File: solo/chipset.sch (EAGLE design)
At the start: 24 parts

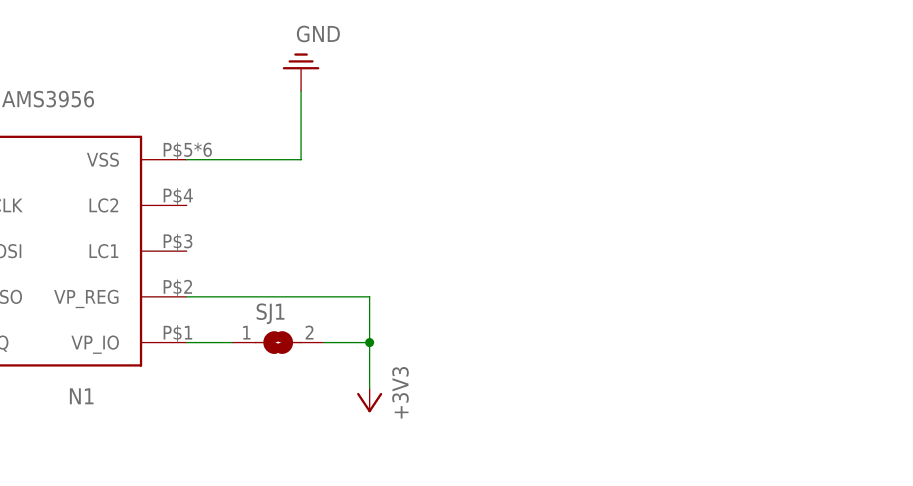
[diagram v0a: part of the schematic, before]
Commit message: add molex nfc antenna/coil
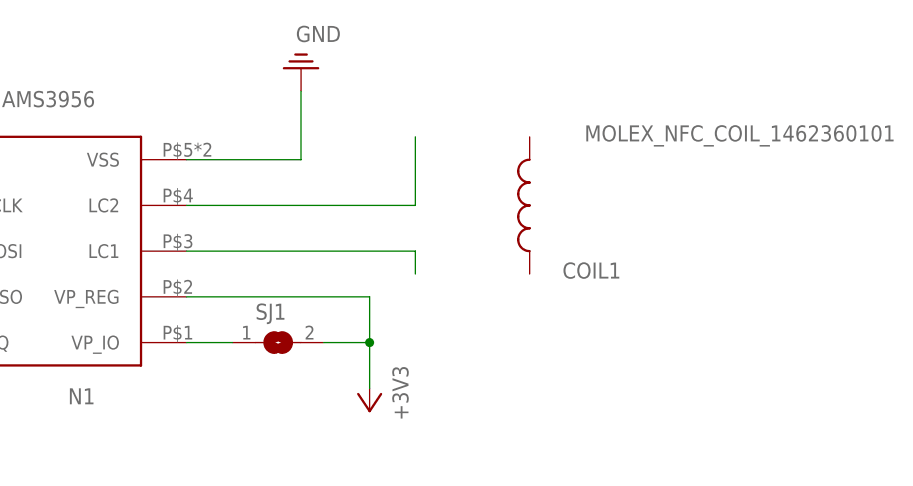
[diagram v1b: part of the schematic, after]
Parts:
- added COIL1: MOLEX_NFC_COIL_1462360101, efm-fido:MOLEX_NFC_COIL_1462360101
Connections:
- new net N$12: N1.LC2
- new net N$13: N1.LC1
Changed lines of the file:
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@@
 <part name="SWCLK" library="efm-fido" library_urn="urn:adsk.eagle:library:4245354" deviceset="TEST_POINT" device="" package3d_urn="urn:adsk.eagle:package:4245792/4"/>
 <part name="R1" library="efm-fido" library_urn="urn:adsk.eagle:library:4245354" deviceset="RESISTOR" device="" package3d_urn="urn:adsk.eagle:package:4245807/6" value="175"/>
-<part name="L1" library="efm-fido" library_urn="urn:adsk.eagle:library:4245354" deviceset="EAST1616RGBA3-LED-RGB" device="CL-505S-X-SD-T" package3d_urn="urn:adsk.eagle:package:4878740/4"/>
+<part name="L1" library="efm-fido" library_urn="urn:adsk.eagle:library:4245354" deviceset="EAST1616RGBA3-LED-RGB" device="CL-505S-X-SD-T" package3d_urn="urn:adsk.eagle:package:4878740/6"/>
 <part name="STX-&gt;" library="efm-fido" library_urn="urn:adsk.eagle:library:4245354" deviceset="TEST_POINT" device="" package3d_urn="urn:adsk.eagle:package:4245792/4"/>
 <part name="SRX&lt;-" library="efm-fido" library_urn="urn:adsk.eagle:library:4245354" deviceset="TEST_POINT" device="" package3d_urn="urn:adsk.eagle:package:4245792/4"/>
@@
 <part name="C6" library="efm-fido" library_urn="urn:adsk.eagle:library:4245354" deviceset="CAPACITOR" device="" package3d_urn="urn:adsk.eagle:package:4245806/7" value="4.7u"/>
 <part name="SUPPLY6" library="supply2" library_urn="urn:adsk.eagle:library:372" deviceset="PE" device="" value="GND"/>
-<part name="ST1" library="efm-fido" library_urn="urn:adsk.eagle:library:4245354" deviceset="STM32L432KCU6" device="" package3d_urn="urn:adsk.eagle:package:4245373/4"/>
+<part name="ST1" library="efm-fido" library_urn="urn:adsk.eagle:library:4245354" deviceset="STM32L432KCU6" device="" package3d_urn="urn:adsk.eagle:package:4245373/6"/>
 <part name="SWO" library="efm-fido" library_urn="urn:adsk.eagle:library:4245354" deviceset="TEST_POINT" device="" package3d_urn="urn:adsk.eagle:package:4245792/4"/>
-<part name="L3" library="efm-fido" library_urn="urn:adsk.eagle:library:4245354" deviceset="NCP114AMX330TCG" device="" package3d_urn="urn:adsk.eagle:package:5621121/2"/>
+<part name="L3" library="efm-fido" library_urn="urn:adsk.eagle:library:4245354" deviceset="NCP114AMX330TCG" device="" package3d_urn="urn:adsk.eagle:package:5621121/3"/>
 <part name="Z1" library="efm-fido" library_urn="urn:adsk.eagle:library:4245354" deviceset="BZA900A-ESD-ZENERS" device="" package3d_urn="urn:adsk.eagle:package:5621120/4"/>
 <part name="P+1" library="supply1" library_urn="urn:adsk.eagle:library:371" deviceset="+5V" device=""/>
@@
 <part name="+3V6" library="supply1" library_urn="urn:adsk.eagle:library:371" deviceset="+3V3" device=""/>
 <part name="+3V7" library="supply1" library_urn="urn:adsk.eagle:library:371" deviceset="+3V3" device=""/>
-<part name="U$1" library="efm-fido" library_urn="urn:adsk.eagle:library:4245354" deviceset="DOME_BUTTON" device="12MM" package3d_urn="urn:adsk.eagle:package:5648519/4"/>
-<part name="N1" library="efm-fido" library_urn="urn:adsk.eagle:library:4245354" deviceset="AMS3956" device="" package3d_urn="urn:adsk.eagle:package:5825738/1"/>
+<part name="U$1" library="efm-fido" library_urn="urn:adsk.eagle:library:4245354" deviceset="DOME_BUTTON" device="12MM" package3d_urn="urn:adsk.eagle:package:5648519/5"/>
+<part name="N1" library="efm-fido" library_urn="urn:adsk.eagle:library:4245354" deviceset="AMS3956" device="" package3d_urn="urn:adsk.eagle:package:5825738/2"/>
 <part name="SUPPLY8" library="supply2" library_urn="urn:adsk.eagle:library:372" deviceset="PE" device="" value="GND"/>
 <part name="+3V8" library="supply1" library_urn="urn:adsk.eagle:library:371" deviceset="+3V3" device=""/>
 <part name="SJ1" library="jumper" library_urn="urn:adsk.eagle:library:252" deviceset="SJ" device="" package3d_urn="urn:adsk.eagle:package:15471/1"/>
+<part name="COIL1" library="efm-fido" library_urn="urn:adsk.eagle:library:4245354" deviceset="MOLEX_NFC_COIL_1462360101" device="" package3d_urn="urn:adsk.eagle:package:7114966/5"/>
 </parts>
 <sheets>
@@
 <attribute name="NAME" x="256.54" y="127" size="1.778" layer="95"/>
 <attribute name="VALUE" x="256.54" y="120.65" size="1.778" layer="96"/>
+</instance>
+<instance part="COIL1" gate="G$1" x="287.02" y="139.7" smashed="yes" rot="R180">
+<attribute name="NAME" x="297.18" y="133.35" size="1.778" layer="95" rot="R180"/>
+<attribute name="VALUE" x="327.66" y="148.59" size="1.778" layer="96" rot="R180"/>
 </instance>
 </instances>
@@
 </segment>
 </net>
+<net name="N$12" class="0">
+<segment>
+<pinref part="N1" gate="G$1" pin="LC2"/>
+<wire x1="248.92" y1="139.7" x2="274.32" y2="139.7" width="0.1524" layer="91"/>
+<wire x1="274.32" y1="139.7" x2="274.32" y2="147.32" width="0.1524" layer="91"/>
+</segment>
+</net>
+<net name="N$13" class="0">
+<segment>
+<pinref part="N1" gate="G$1" pin="LC1"/>
+<wire x1="248.92" y1="134.62" x2="274.32" y2="134.62" width="0.1524" layer="91"/>
+<wire x1="274.32" y1="134.62" x2="274.32" y2="132.08" width="0.1524" layer="91"/>
+</segment>
+</net>

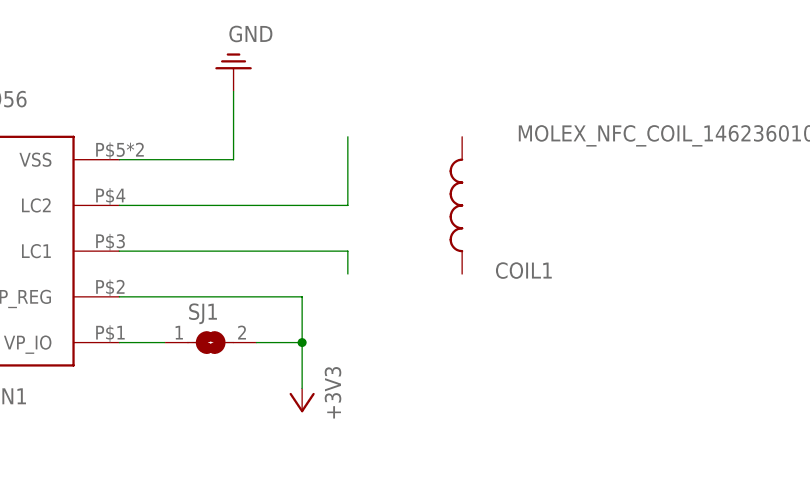
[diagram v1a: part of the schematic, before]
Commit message: update chipset
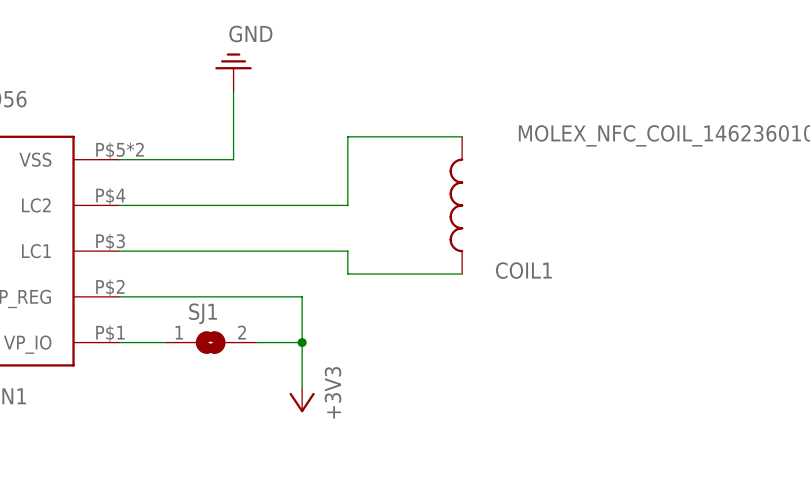
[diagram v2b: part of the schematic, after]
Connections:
- net N$12: now also COIL1.2
- net N$13: now also COIL1.1
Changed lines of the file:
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@@
 <wire x1="248.92" y1="139.7" x2="274.32" y2="139.7" width="0.1524" layer="91"/>
 <wire x1="274.32" y1="139.7" x2="274.32" y2="147.32" width="0.1524" layer="91"/>
+<pinref part="COIL1" gate="G$1" pin="2"/>
+<wire x1="274.32" y1="147.32" x2="287.02" y2="147.32" width="0.1524" layer="91"/>
 </segment>
 </net>
@@
 <wire x1="248.92" y1="134.62" x2="274.32" y2="134.62" width="0.1524" layer="91"/>
 <wire x1="274.32" y1="134.62" x2="274.32" y2="132.08" width="0.1524" layer="91"/>
+<pinref part="COIL1" gate="G$1" pin="1"/>
+<wire x1="287.02" y1="132.08" x2="274.32" y2="132.08" width="0.1524" layer="91"/>
 </segment>
 </net>
